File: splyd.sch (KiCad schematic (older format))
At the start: 74 parts, among them J0 AudioJack3, J1 USB from Pro micro, K00 KEYSW, K01 KEYSW, K02 KEYSW, K03 KEYSW, K04 KEYSW, K05 KEYSW, K10 KEYSW, K11 KEYSW, K12 KEYSW, K13 KEYSW, K14 KEYSW, K15 KEYSW, K16 KEYSW, K20 KEYSW, K21 KEYSW, K22 KEYSW, K23 KEYSW, K24 KEYSW, K25 KEYSW, K26 KEYSW, K30 KEYSW, K31 KEYSW, K32 KEYSW, K33 KEYSW, K34 KEYSW, K35 KEYSW, K36 KEYSW, K43 KEYSW, K44 KEYSW, K45 KEYSW, K46 KEYSW, K54 KEYSW, K55 KEYSW, K56 KEYSW, U0 Pro Micro

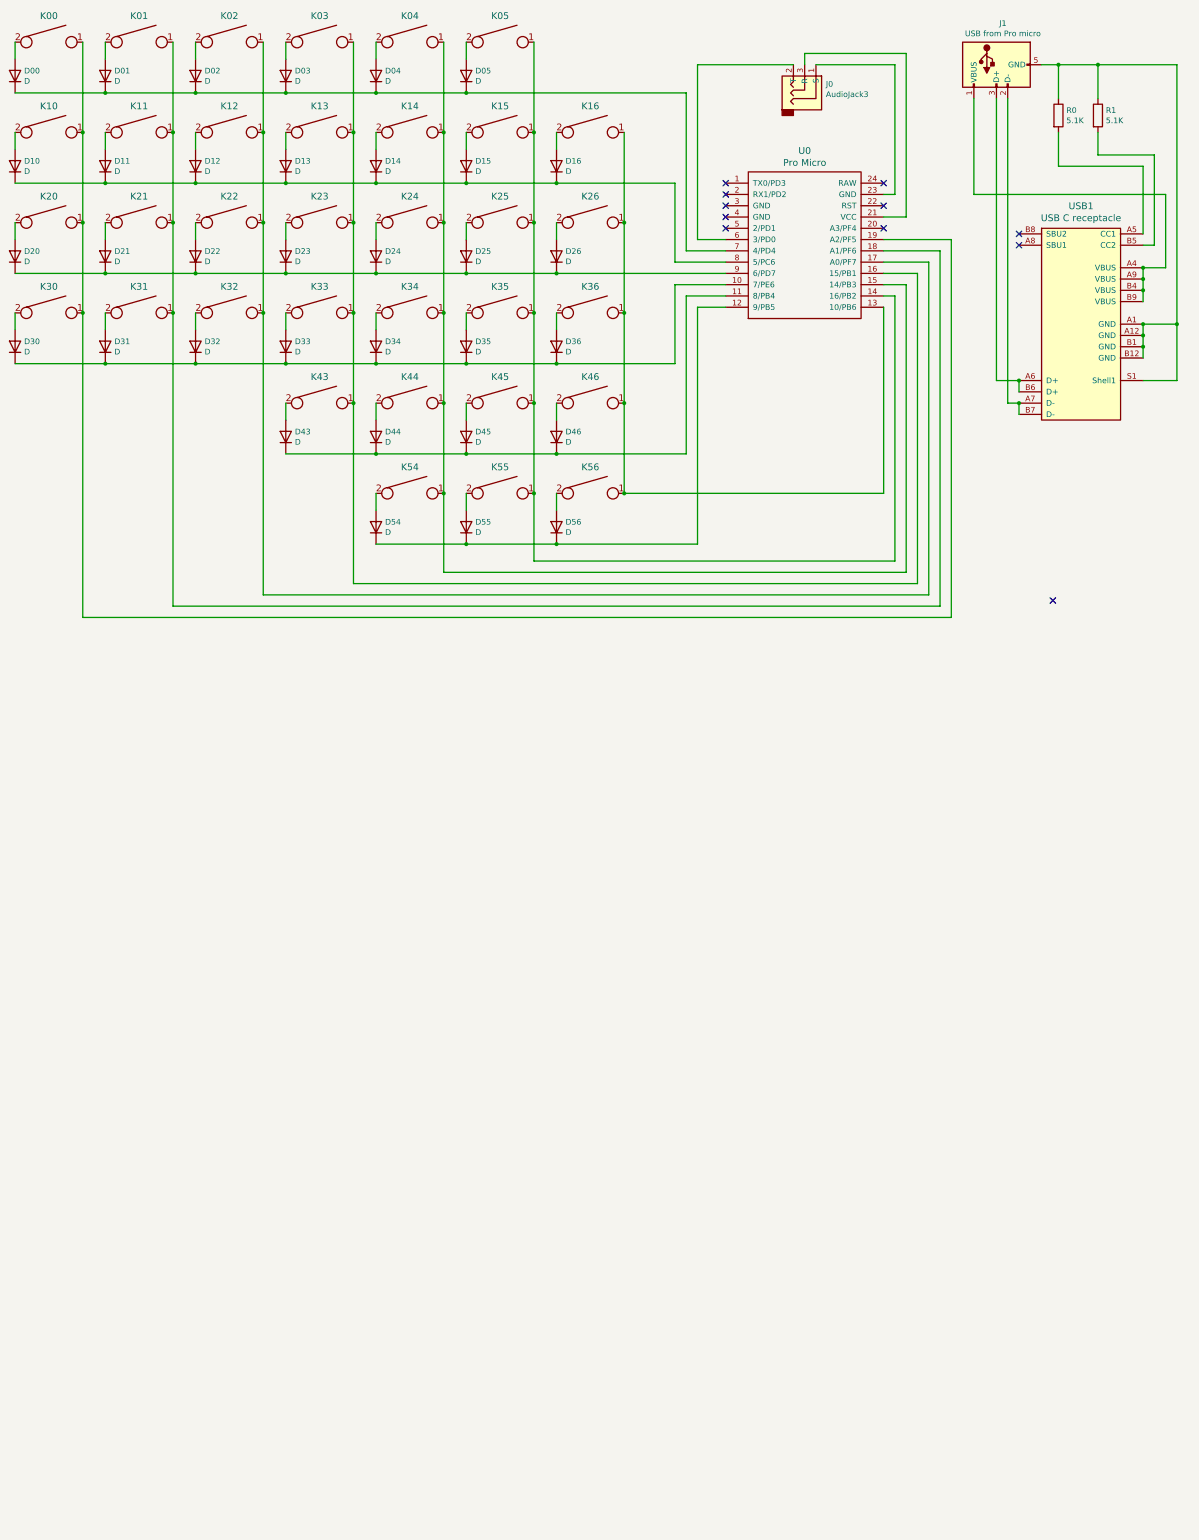
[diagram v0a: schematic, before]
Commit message: Add right hand and prepare footprint placements
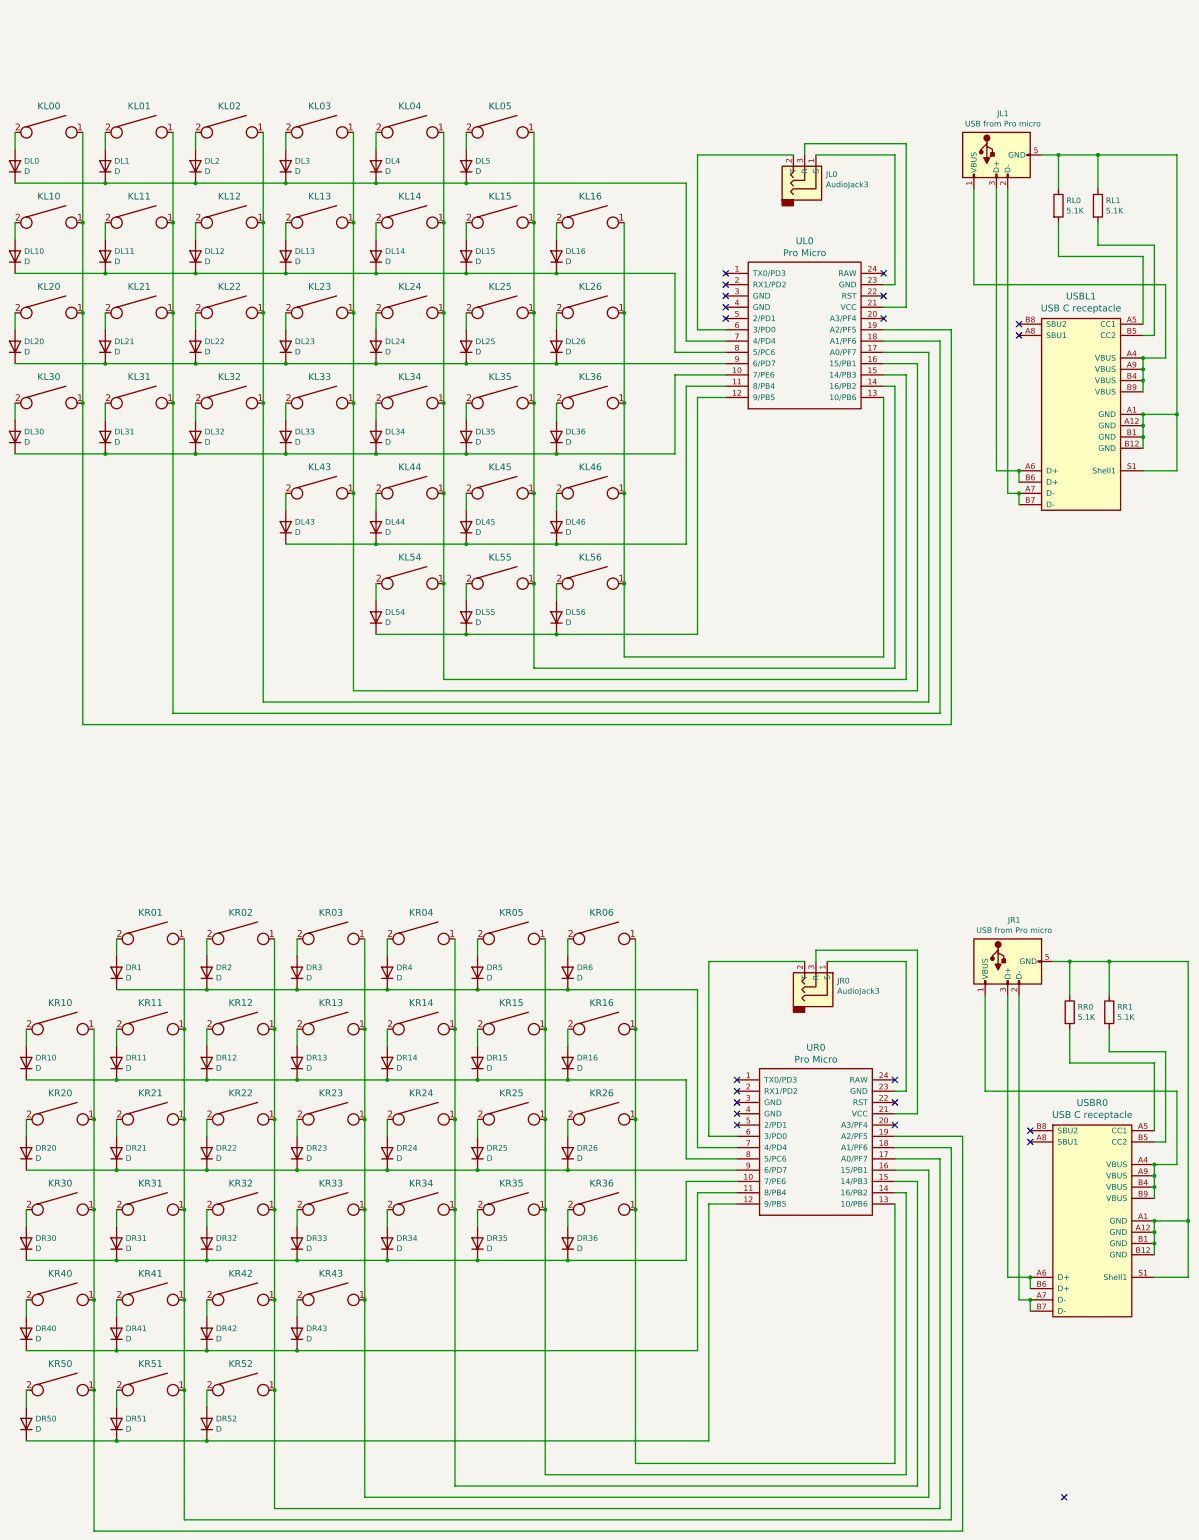
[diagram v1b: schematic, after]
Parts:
- added DR1, DR10, DR11, DR12, DR13, DR14, DR15, DR16, DR2, DR20, DR21, DR22, DR23, DR24, DR25, DR26, DR3, DR30, DR31, DR32, DR33, DR34, DR35, DR36, DR4, DR40, DR41, DR42, DR43, DR5, DR50, DR51, DR52, DR6: D, keyboard_parts:D_SOD123_axial, symbol Device:D
- added JR0: AudioJack3, mod_conn_av:jack_3.5_pj313d-smt, symbol Connector:AudioJack3
- added JR1: USB from Pro micro, Connector_Wire:Pad_1x04_SMD_1x2mm, symbol Connector:Micro_USB_wires
- added KR01, KR02, KR03, KR04, KR05, KR06, KR10, KR11, KR12, KR13, KR14, KR15, KR16, KR20, KR21, KR22, KR23, KR24, KR25, KR26, KR30, KR31, KR32, KR33, KR34, KR35, KR36, KR40, KR41, KR42, KR43, KR50, KR51, KR52: KEYSW, keyswitches:Kailh_socket_MX, symbol keyboard_parts:KEYSW
- added RR0, RR1: 5.1K, Resistor_SMD:R_0603_1608Metric, symbol Device:R
- added UR0: Pro Micro, Keebio-Parts:ArduinoProMicro-ZigZag, symbol keebio:ProMicro
- added USBR0: USB C receptacle, Type-C:USB_C_GCT_USB4085, symbol Type-C:USB_C_GCT_USB4085
- renumbered D00 to DL0, D01 to DL1, D10 to DL10, D11 to DL11, D12 to DL12, D13 to DL13, D14 to DL14, D15 to DL15, D16 to DL16, D02 to DL2, D20 to DL20, D21 to DL21, D22 to DL22, D23 to DL23, D24 to DL24, D25 to DL25, D26 to DL26, D03 to DL3, D30 to DL30, D31 to DL31, D32 to DL32, D33 to DL33, D34 to DL34, D35 to DL35, D36 to DL36, D04 to DL4, D43 to DL43, D44 to DL44, D45 to DL45, D46 to DL46, D05 to DL5, D54 to DL54, D55 to DL55, D56 to DL56, J0 to JL0, J1 to JL1, K00 to KL00, K01 to KL01, K02 to KL02, K03 to KL03, K04 to KL04, K05 to KL05, K10 to KL10, K11 to KL11, K12 to KL12, K13 to KL13, K14 to KL14, K15 to KL15, K16 to KL16, K20 to KL20, K21 to KL21, K22 to KL22, K23 to KL23, K24 to KL24, K25 to KL25, K26 to KL26, K30 to KL30, K31 to KL31, K32 to KL32, K33 to KL33, K34 to KL34, K35 to KL35, K36 to KL36, K43 to KL43, K44 to KL44, K45 to KL45, K46 to KL46, K54 to KL54, K55 to KL55, K56 to KL56, R0 to RL0, R1 to RL1, U0 to UL0, USB1 to USBL1
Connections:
- new net: JR1.5 (GND), RR0.1, RR1.1, USBR0.A1 (GND), USBR0.A12 (GND), USBR0.B1 (GND), USBR0.B12 (GND), USBR0.S1 (Shell1)
- new net: JR1.1 (VBUS), USBR0.A4 (VBUS), USBR0.A9 (VBUS), USBR0.B4 (VBUS), USBR0.B9 (VBUS)
- new net: RR0.2, USBR0.A5 (CC1)
- new net: JR1.3 (D+), USBR0.A6 (D+), USBR0.B6 (D+)
- new net: JR1.2 (D-), USBR0.A7 (D-), USBR0.B7 (D-)
- new net: RR1.2, USBR0.B5 (CC2)
- new net: DR30.1 (K), DR31.1 (K), DR32.1 (K), DR33.1 (K), DR34.1 (K), DR35.1 (K), DR36.1 (K), UR0.10 (7/PE6)
- new net: DR40.1 (K), DR41.1 (K), DR42.1 (K), DR43.1 (K), UR0.11 (8/PB4)
- new net: DR50.1 (K), DR51.1 (K), DR52.1 (K), UR0.12 (9/PB5)
- new net: KR06.1, KR16.1, KR26.1, KR36.1, UR0.13 (10/PB6)
- new net: KR05.1, KR15.1, KR25.1, KR35.1, UR0.14 (16/PB2)
- new net: KR04.1, KR14.1, KR24.1, KR34.1, UR0.15 (14/PB3)
- new net: KR03.1, KR13.1, KR23.1, KR33.1, KR43.1, UR0.16 (15/PB1)
- new net: KR02.1, KR12.1, KR22.1, KR32.1, KR42.1, KR52.1, UR0.17 (A0/PF7)
- new net: KR01.1, KR11.1, KR21.1, KR31.1, KR41.1, KR51.1, UR0.18 (A1/PF6)
- new net: KR10.1, KR20.1, KR30.1, KR40.1, KR50.1, UR0.19 (A2/PF5)
- new net: JR0.3 (R), UR0.21 (VCC)
- new net: JR0.1 (S), UR0.23 (GND)
- new net: JR0.2 (T), UR0.6 (3/PD0)
- new net: DR1.1 (K), DR2.1 (K), DR3.1 (K), DR4.1 (K), DR5.1 (K), DR6.1 (K), UR0.7 (4/PD4)
- new net: DR10.1 (K), DR11.1 (K), DR12.1 (K), DR13.1 (K), DR14.1 (K), DR15.1 (K), DR16.1 (K), UR0.8 (5/PC6)
- new net: DR20.1 (K), DR21.1 (K), DR22.1 (K), DR23.1 (K), DR24.1 (K), DR25.1 (K), DR26.1 (K), UR0.9 (6/PD7)
- new net: DR52.2 (A), KR52.2
- new net: DR43.2 (A), KR43.2
- new net: DR51.2 (A), KR51.2
- new net: DR50.2 (A), KR50.2
- new net: DR42.2 (A), KR42.2
- new net: DR41.2 (A), KR41.2
- new net: DR40.2 (A), KR40.2
- new net: DR36.2 (A), KR36.2
- new net: DR26.2 (A), KR26.2
- new net: DR35.2 (A), KR35.2
- new net: DR34.2 (A), KR34.2
- new net: DR25.2 (A), KR25.2
- new net: DR24.2 (A), KR24.2
- new net: DR33.2 (A), KR33.2
- new net: DR32.2 (A), KR32.2
- new net: DR23.2 (A), KR23.2
- new net: DR22.2 (A), KR22.2
- new net: DR31.2 (A), KR31.2
- new net: DR30.2 (A), KR30.2
- new net: DR21.2 (A), KR21.2
- new net: DR20.2 (A), KR20.2
- new net: DR16.2 (A), KR16.2
- new net: DR15.2 (A), KR15.2
- new net: DR14.2 (A), KR14.2
- new net: DR6.2 (A), KR06.2
- new net: DR5.2 (A), KR05.2
- new net: DR13.2 (A), KR13.2
- new net: DR12.2 (A), KR12.2
- new net: DR4.2 (A), KR04.2
- new net: DR3.2 (A), KR03.2
- new net: DR11.2 (A), KR11.2
- new net: DR10.2 (A), KR10.2
- new net: DR2.2 (A), KR02.2
- new net: DR1.2 (A), KR01.2
- no-connect marks 11 -> 21
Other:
- moved on the sheet: DL0, DL1, DL10, DL11, DL12, DL13, DL14, DL15, DL16, DL2, DL20, DL21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

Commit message: Keyswitch footprint with window and 3rd time routing
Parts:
- KL00, KL01, KL02, KL03, KL04, KL05, KL10, KL11, KL12, KL13, KL14, KL15, KL16, KL20, KL21, KL22, KL23, KL24, KL25, KL26, KL30, KL31, KL32, KL33, KL34, KL35, KL36, KL43, KL44, KL45, KL46, KL54, KL55, KL56, KR01, KR02, KR03, KR04, KR05, KR06, KR10, KR11, KR12, KR13, KR14, KR15, KR16, KR20, KR21, KR22, KR23, KR24, KR25, KR26, KR30, KR31, KR32, KR33, KR34, KR35, KR36, KR40, KR41, KR42, KR43, KR50, KR51, KR52: footprint keyswitches:Kailh_socket_MX -> keyswitches:Kailh_socket_MX--window

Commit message: Wire key RGB diodes for right thumb cluster
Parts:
- removed DL0, DL1, DL2, DL3, DL4, DL5, DR1, DR2, DR3, DR4, DR5, DR6: D, keyboard_parts:D_SOD123_axial, symbol Device:D
- removed KL00, KL01, KL02, KL03, KL04, KL05, KR01, KR02, KR03, KR04, KR05, KR06: KEYSW, keyswitches:Kailh_socket_MX--window, symbol keyboard_parts:KEYSW
- added CL00, CL01, CL02, CL03, CL04, CL05, CL06, CL10, CL11, CL12, CL13, CL14, CL15, CL16, CL20, CL21, CL22, CL23, CL24, CL25, CL26, CL33, CL34, CL35, CL36, CL44, CL45, CL46, CLBC_32, CLBL_33, CLBR_29, CLTC_31, CLTL_34, CLTR_30, CR00, CR01, CR02, CR03, CR04, CR05, CR06, CR10, CR11, CR12, CR13, CR14, CR15, CR16, CR20, CR21, CR22, CR23, CR24, CR25, CR26, CR30, CR31, CR32, CR33, CR40, CR41, CR42, CRBC_30, CRBL_29, CRBR_33, CRTC_31, CRTL_30, CRTR_34: C_Small, Capacitor_SMD:C_0603_1608Metric_Pad1.05x0.95mm_HandSolder, symbol Device:C_Small
- added DL00_1, DL01_6, DL02_7, DL03_12, DL04_13, DL05_18, DL06_19, DL10_2, DL11_5, DL12_8, DL13_11, DL14_14, DL15_17, DL16_20, DL20_3, DL21_4, DL22_9, DL23_10, DL24_15, DL25_16, DL26_21, DL33_28, DL34_27, DL35_24, DL36_23, DL44_26, DL45_25, DL46_22, DR00_19, DR01_18, DR02_13, DR03_12, DR04_7, DR05_6, DR06_1, DR10_20, DR11_17, DR12_14, DR13_11, DR14_8, DR15_5, DR16_2, DR20_21, DR21_16, DR22_15, DR23_10, DR24_9, DR25_4, DR26_3, DR30_23, DR31_24, DR32_27, DR33_28, DR40_22, DR41_25, DR42_26: SK6812MINI, keyboard_parts:SK6812MINIE-simple, symbol LED:SK6812MINI
- added DLBC_32, DLBL_33, DLBR_29, DLTC_31, DLTL_34, DLTR_30, DRBC_32, DRBL_29, DRBR_33, DRTC_31, DRTL_30, DRTR_34: SK6812MINI, keyboard_parts:SK6812MINIE-simple_no-hole, symbol LED:SK6812MINI
- JL0, JR0: footprint mod_conn_av:jack_3.5_pj313d-smt -> Keebio-Parts:TRS-PJ-320B
- KL00: renamed from KL10; footprint keyswitches:Kailh_socket_MX--window -> keyswitches:Kailh_socket_MX--space
- KL01: renamed from KL11; footprint keyswitches:Kailh_socket_MX--window -> keyswitches:Kailh_socket_MX--space
- KL02: renamed from KL12; footprint keyswitches:Kailh_socket_MX--window -> keyswitches:Kailh_socket_MX--space
- KL03: renamed from KL13; footprint keyswitches:Kailh_socket_MX--window -> keyswitches:Kailh_socket_MX--space
- KL04: renamed from KL14; footprint keyswitches:Kailh_socket_MX--window -> keyswitches:Kailh_socket_MX--space
- KL05: renamed from KL15; footprint keyswitches:Kailh_socket_MX--window -> keyswitches:Kailh_socket_MX--space
- KL06: renamed from KL16; footprint keyswitches:Kailh_socket_MX--window -> keyswitches:Kailh_socket_MX--space
- KL10: renamed from KL20; footprint keyswitches:Kailh_socket_MX--window -> keyswitches:Kailh_socket_MX--space
- KL11: renamed from KL21; footprint keyswitches:Kailh_socket_MX--window -> keyswitches:Kailh_socket_MX--space
- KL12: renamed from KL22; footprint keyswitches:Kailh_socket_MX--window -> keyswitches:Kailh_socket_MX--space
- KL13: renamed from KL23; footprint keyswitches:Kailh_socket_MX--window -> keyswitches:Kailh_socket_MX--space
- KL14: renamed from KL24; footprint keyswitches:Kailh_socket_MX--window -> keyswitches:Kailh_socket_MX--space
- KL15: renamed from KL25; footprint keyswitches:Kailh_socket_MX--window -> keyswitches:Kailh_socket_MX--space
- KL16: renamed from KL26; footprint keyswitches:Kailh_socket_MX--window -> keyswitches:Kailh_socket_MX--space
- KL20: renamed from KL30; footprint keyswitches:Kailh_socket_MX--window -> keyswitches:Kailh_socket_MX--space
- KL21: renamed from KL31; footprint keyswitches:Kailh_socket_MX--window -> keyswitches:Kailh_socket_MX--space
- KL22: renamed from KL32; footprint keyswitches:Kailh_socket_MX--window -> keyswitches:Kailh_socket_MX--space
- KL23: renamed from KL33; footprint keyswitches:Kailh_socket_MX--window -> keyswitches:Kailh_socket_MX--space
- KL24: renamed from KL34; footprint keyswitches:Kailh_socket_MX--window -> keyswitches:Kailh_socket_MX--space
- KL25: renamed from KL35; footprint keyswitches:Kailh_socket_MX--window -> keyswitches:Kailh_socket_MX--space
- KL26: renamed from KL36; footprint keyswitches:Kailh_socket_MX--window -> keyswitches:Kailh_socket_MX--space
- KL33: renamed from KL43; footprint keyswitches:Kailh_socket_MX--window -> keyswitches:Kailh_socket_MX--space
- KL34: renamed from KL44; footprint keyswitches:Kailh_socket_MX--window -> keyswitches:Kailh_socket_MX--space
- KL35: renamed from KL45; footprint keyswitches:Kailh_socket_MX--window -> keyswitches:Kailh_socket_MX--space
- KL36: renamed from KL46; footprint keyswitches:Kailh_socket_MX--window -> keyswitches:Kailh_socket_MX--space
- KL44: renamed from KL54; footprint keyswitches:Kailh_socket_MX--window -> keyswitches:Kailh_socket_MX--space
- KL45: renamed from KL55; footprint keyswitches:Kailh_socket_MX--window -> keyswitches:Kailh_socket_MX--space
- KL46: renamed from KL56; footprint keyswitches:Kailh_socket_MX--window -> keyswitches:Kailh_socket_MX--space
- KR00: renamed from KR10; footprint keyswitches:Kailh_socket_MX--window -> keyswitches:Kailh_socket_MX--space
- KR01: renamed from KR11; footprint keyswitches:Kailh_socket_MX--window -> keyswitches:Kailh_socket_MX--space
- KR02: renamed from KR12; footprint keyswitches:Kailh_socket_MX--window -> keyswitches:Kailh_socket_MX--space
- KR03: renamed from KR13; footprint keyswitches:Kailh_socket_MX--window -> keyswitches:Kailh_socket_MX--space
- KR04: renamed from KR14; footprint keyswitches:Kailh_socket_MX--window -> keyswitches:Kailh_socket_MX--space
- KR05: renamed from KR15; footprint keyswitches:Kailh_socket_MX--window -> keyswitches:Kailh_socket_MX--space
- KR06: renamed from KR16; footprint keyswitches:Kailh_socket_MX--window -> keyswitches:Kailh_socket_MX--space
- KR10: renamed from KR20; footprint keyswitches:Kailh_socket_MX--window -> keyswitches:Kailh_socket_MX--space
- KR11: renamed from KR21; footprint keyswitches:Kailh_socket_MX--window -> keyswitches:Kailh_socket_MX--space
- KR12: renamed from KR22; footprint keyswitches:Kailh_socket_MX--window -> keyswitches:Kailh_socket_MX--space
- KR13: renamed from KR23; footprint keyswitches:Kailh_socket_MX--window -> keyswitches:Kailh_socket_MX--space
- KR14: renamed from KR24; footprint keyswitches:Kailh_socket_MX--window -> keyswitches:Kailh_socket_MX--space
- KR15: renamed from KR25; footprint keyswitches:Kailh_socket_MX--window -> keyswitches:Kailh_socket_MX--space
- KR16: renamed from KR26; footprint keyswitches:Kailh_socket_MX--window -> keyswitches:Kailh_socket_MX--space
- KR20: renamed from KR30; footprint keyswitches:Kailh_socket_MX--window -> keyswitches:Kailh_socket_MX--space
- KR21: renamed from KR31; footprint keyswitches:Kailh_socket_MX--window -> keyswitches:Kailh_socket_MX--space
- KR22: renamed from KR32; footprint keyswitches:Kailh_socket_MX--window -> keyswitches:Kailh_socket_MX--space
- KR23: renamed from KR33; footprint keyswitches:Kailh_socket_MX--window -> keyswitches:Kailh_socket_MX--space
- KR24: renamed from KR34; footprint keyswitches:Kailh_socket_MX--window -> keyswitches:Kailh_socket_MX--space
- KR25: renamed from KR35; footprint keyswitches:Kailh_socket_MX--window -> keyswitches:Kailh_socket_MX--space
- KR26: renamed from KR36; footprint keyswitches:Kailh_socket_MX--window -> keyswitches:Kailh_socket_MX--space
- KR30: renamed from KR40; footprint keyswitches:Kailh_socket_MX--window -> keyswitches:Kailh_socket_MX--space
- KR31: renamed from KR41; footprint keyswitches:Kailh_socket_MX--window -> keyswitches:Kailh_socket_MX--space
- KR32: renamed from KR42; footprint keyswitches:Kailh_socket_MX--window -> keyswitches:Kailh_socket_MX--space
- KR33: renamed from KR43; footprint keyswitches:Kailh_socket_MX--window -> keyswitches:Kailh_socket_MX--space
- KR40: renamed from KR50; footprint keyswitches:Kailh_socket_MX--window -> keyswitches:Kailh_socket_MX--space
- KR41: renamed from KR51; footprint keyswitches:Kailh_socket_MX--window -> keyswitches:Kailh_socket_MX--space
- KR42: renamed from KR52; footprint keyswitches:Kailh_socket_MX--window -> keyswitches:Kailh_socket_MX--space
- renumbered DL10 to DL00, DL11 to DL01, DL12 to DL02, DL13 to DL03, DL14 to DL04, DL15 to DL05, DL16 to DL06, DL20 to DL10, DL21 to DL11, DL22 to DL12, DL23 to DL13, DL24 to DL14, DL25 to DL15, DL26 to DL16, DL30 to DL20, DL31 to DL21, DL32 to DL22, DL33 to DL23, DL34 to DL24, DL35 to DL25, DL36 to DL26, DL43 to DL33, DL44 to DL34, DL45 to DL35, DL46 to DL36, DL54 to DL44, DL55 to DL45, DL56 to DL46, DR10 to DR00, DR11 to DR01, DR12 to DR02, DR13 to DR03, DR14 to DR04, DR15 to DR05, DR16 to DR06, DR20 to DR10, DR21 to DR11, DR22 to DR12, DR23 to DR13, DR24 to DR14, DR25 to DR15, DR26 to DR16, DR30 to DR20, DR31 to DR21, DR32 to DR22, DR33 to DR23, DR34 to DR24, DR35 to DR25, DR36 to DR26, DR40 to DR30, DR41 to DR31, DR42 to DR32, DR43 to DR33, DR50 to DR40, DR51 to DR41, DR52 to DR42
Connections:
- net LLED: now reaches UL0.1 (TX0/PD3)
- net LLED: now also DLBR_29.3 (DIN)
- net L5V: now reaches JL0.3 (R), UL0.21 (VCC)
- net L5V: now also CL00.1, CL01.1, CL02.1, CL03.1, CL04.1, CL05.1, CL06.1, CL10.1, CL11.1, CL12.1, CL13.1, CL14.1, CL15.1, CL16.1, CL20.1, CL21.1, CL22.1, CL23.1, CL24.1, CL25.1, CL26.1, CL33.1, CL34.1, CL35.1, CL36.1, CL44.1, CL45.1, CL46.1, CLBC_32.1, CLBL_33.1, CLBR_29.1, CLTC_31.1, CLTL_34.1, CLTR_30.1, DL00_1.4 (VDD), DL01_6.4 (VDD), DL02_7.4 (VDD), DL03_12.4 (VDD), DL04_13.4 (VDD), DL05_18.4 (VDD), DL06_19.4 (VDD), DL10_2.4 (VDD), DL11_5.4 (VDD), DL12_8.4 (VDD), DL13_11.4 (VDD), DL14_14.4 (VDD), DL15_17.4 (VDD), DL16_20.4 (VDD), DL20_3.4 (VDD), DL21_4.4 (VDD), DL22_9.4 (VDD), DL23_10.4 (VDD), DL24_15.4 (VDD), DL25_16.4 (VDD), DL26_21.4 (VDD), DL33_28.4 (VDD), DL34_27.4 (VDD), DL35_24.4 (VDD), DL36_23.4 (VDD), DL44_26.4 (VDD), DL45_25.4 (VDD), DL46_22.4 (VDD), DLBC_32.4 (VDD), DLBL_33.4 (VDD), DLBR_29.4 (VDD), DLTC_31.4 (VDD), DLTL_34.4 (VDD), DLTR_30.4 (VDD)
- net GND1: now reaches JL0.1 (S), UL0.23 (GND)
- net GND1: now also CL00.2, CL01.2, CL02.2, CL03.2, CL04.2, CL05.2, CL06.2, CL10.2, CL11.2, CL12.2, CL13.2, CL14.2, CL15.2, CL16.2, CL20.2, CL21.2, CL22.2, CL23.2, CL24.2, CL25.2, CL26.2, CL33.2, CL34.2, CL35.2, CL36.2, CL44.2, CL45.2, CL46.2, CLBC_32.2, CLBL_33.2, CLBR_29.2, CLTC_31.2, CLTL_34.2, CLTR_30.2, DL00_1.2 (VSS), DL01_6.2 (VSS), DL02_7.2 (VSS), DL03_12.2 (VSS), DL04_13.2 (VSS), DL05_18.2 (VSS), DL06_19.2 (VSS), DL10_2.2 (VSS), DL11_5.2 (VSS), DL12_8.2 (VSS), DL13_11.2 (VSS), DL14_14.2 (VSS), DL15_17.2 (VSS), DL16_20.2 (VSS), DL20_3.2 (VSS), DL21_4.2 (VSS), DL22_9.2 (VSS), DL23_10.2 (VSS), DL24_15.2 (VSS), DL25_16.2 (VSS), DL26_21.2 (VSS), DL33_28.2 (VSS), DL34_27.2 (VSS), DL35_24.2 (VSS), DL36_23.2 (VSS), DL44_26.2 (VSS), DL45_25.2 (VSS), DL46_22.2 (VSS), DLBC_32.2 (VSS), DLBL_33.2 (VSS), DLBR_29.2 (VSS), DLTC_31.2 (VSS), DLTL_34.2 (VSS), DLTR_30.2 (VSS)
- net RLED: now reaches UR0.1 (TX0/PD3)
- net RLED: now also DRBL_29.3 (DIN)
- net R5V: now reaches JR0.3 (R), UR0.21 (VCC)
- net R5V: now also CR00.1, CR01.1, CR02.1, CR03.1, CR04.1, CR05.1, CR06.1, CR10.1, CR11.1, CR12.1, CR13.1, CR14.1, CR15.1, CR16.1, CR20.1, CR21.1, CR22.1, CR23.1, CR24.1, CR25.1, CR26.1, CR30.1, CR31.1, CR32.1, CR33.1, CR40.1, CR41.1, CR42.1, CRBC_30.1, CRBL_29.1, CRBR_33.1, CRTC_31.1, CRTL_30.1, CRTR_34.1, DR00_19.4 (VDD), DR01_18.4 (VDD), DR02_13.4 (VDD), DR03_12.4 (VDD), DR04_7.4 (VDD), DR05_6.4 (VDD), DR06_1.4 (VDD), DR10_20.4 (VDD), DR11_17.4 (VDD), DR12_14.4 (VDD), DR13_11.4 (VDD), DR14_8.4 (VDD), DR15_5.4 (VDD), DR16_2.4 (VDD), DR20_21.4 (VDD), DR21_16.4 (VDD), DR22_15.4 (VDD), DR23_10.4 (VDD), DR24_9.4 (VDD), DR25_4.4 (VDD), DR26_3.4 (VDD), DR30_23.4 (VDD), DR31_24.4 (VDD), DR32_27.4 (VDD), DR33_28.4 (VDD), DR40_22.4 (VDD), DR41_25.4 (VDD), DR42_26.4 (VDD), DRBC_32.4 (VDD), DRBL_29.4 (VDD), DRBR_33.4 (VDD), DRTC_31.4 (VDD), DRTL_30.4 (VDD), DRTR_34.4 (VDD)
- net GND2: now reaches JR0.1 (S), UR0.23 (GND)
- net GND2: now also CR00.2, CR01.2, CR02.2, CR03.2, CR04.2, CR05.2, CR06.2, CR10.2, CR11.2, CR12.2, CR13.2, CR14.2, CR15.2, CR16.2, CR20.2, CR21.2, CR22.2, CR23.2, CR24.2, CR25.2, CR26.2, CR30.2, CR31.2, CR32.2, CR33.2, CR40.2, CR41.2, CR42.2, CRBC_30.2, CRBL_29.2, CRBR_33.2, CRTC_31.2, CRTL_30.2, CRTR_34.2, DR00_19.2 (VSS), DR01_18.2 (VSS), DR02_13.2 (VSS), DR03_12.2 (VSS), DR04_7.2 (VSS), DR05_6.2 (VSS), DR06_1.2 (VSS), DR10_20.2 (VSS), DR11_17.2 (VSS), DR12_14.2 (VSS), DR13_11.2 (VSS), DR14_8.2 (VSS), DR15_5.2 (VSS), DR16_2.2 (VSS), DR20_21.2 (VSS), DR21_16.2 (VSS), DR22_15.2 (VSS), DR23_10.2 (VSS), DR24_9.2 (VSS), DR25_4.2 (VSS), DR26_3.2 (VSS), DR30_23.2 (VSS), DR31_24.2 (VSS), DR32_27.2 (VSS), DR33_28.2 (VSS), DR40_22.2 (VSS), DR41_25.2 (VSS), DR42_26.2 (VSS), DRBC_32.2 (VSS), DRBL_29.2 (VSS), DRBR_33.2 (VSS), DRTC_31.2 (VSS), DRTL_30.2 (VSS), DRTR_34.2 (VSS)
- new net: DL00_1.1 (DOUT), DL10_2.3 (DIN)
- new net: DL00_1.3 (DIN), DLTL_34.1 (DOUT)
- new net: DL10_2.1 (DOUT), DL20_3.3 (DIN)
- new net: DL20_3.1 (DOUT), DL21_4.3 (DIN)
- new net: DL01_6.1 (DOUT), DL02_7.3 (DIN)
- new net: DL01_6.3 (DIN), DL11_5.1 (DOUT)
- new net: DL11_5.3 (DIN), DL21_4.1 (DOUT)
- new net: DL02_7.1 (DOUT), DL12_8.3 (DIN)
- new net: DL12_8.1 (DOUT), DL22_9.3 (DIN)
- new net: DL22_9.1 (DOUT), DL23_10.3 (DIN)
- new net: DL03_12.1 (DOUT), DL04_13.3 (DIN)
- new net: DL03_12.3 (DIN), DL13_11.1 (DOUT)
- new net: DL13_11.3 (DIN), DL23_10.1 (DOUT)
- new net: DL33_28.3 (DIN), DL34_27.1 (DOUT)
- new net: DL04_13.1 (DOUT), DL14_14.3 (DIN)
- new net: DL14_14.1 (DOUT), DL24_15.3 (DIN)
- new net: DL24_15.1 (DOUT), DL25_16.3 (DIN)
- new net: DL34_27.3 (DIN), DL44_26.1 (DOUT)
- new net: DL44_26.3 (DIN), DL45_25.1 (DOUT)
- new net: DL05_18.1 (DOUT), DL06_19.3 (DIN)
- new net: DL05_18.3 (DIN), DL15_17.1 (DOUT)
- new net: DL15_17.3 (DIN), DL25_16.1 (DOUT)
- new net: DL35_24.1 (DOUT), DL45_25.3 (DIN)
- new net: DL35_24.3 (DIN), DL36_23.1 (DOUT)
- new net: DL06_19.1 (DOUT), DL16_20.3 (DIN)
- new net: DL16_20.1 (DOUT), DL26_21.3 (DIN)
- new net: DL26_21.1 (DOUT), DL46_22.3 (DIN)
- new net: DL36_23.3 (DIN), DL46_22.1 (DOUT)
- new net: DLBL_33.1 (DOUT), DLTL_34.3 (DIN)
- new net: DLBC_32.1 (DOUT), DLBL_33.3 (DIN)
- new net: DLBC_32.3 (DIN), DLTC_31.1 (DOUT)
- new net: DLTC_31.3 (DIN), DLTR_30.1 (DOUT)
- new net: DLBR_29.1 (DOUT), DLTR_30.3 (DIN)
- new net: DR00_19.1 (DOUT), DR10_20.3 (DIN)
- new net: DR00_19.3 (DIN), DR01_18.1 (DOUT)
- new net: DR10_20.1 (DOUT), DR20_21.3 (DIN)
- new net: DR20_21.1 (DOUT), DR40_22.3 (DIN)
- new net: DR30_23.1 (DOUT), DR31_24.3 (DIN)
- new net: DR30_23.3 (DIN), DR40_22.1 (DOUT)
- new net: DR01_18.3 (DIN), DR11_17.1 (DOUT)
- new net: DR11_17.3 (DIN), DR21_16.1 (DOUT)
- new net: DR21_16.3 (DIN), DR22_15.1 (DOUT)
- new net: DR31_24.1 (DOUT), DR41_25.3 (DIN)
- new net: DR41_25.1 (DOUT), DR42_26.3 (DIN)
- new net: DR02_13.1 (DOUT), DR12_14.3 (DIN)
- new net: DR02_13.3 (DIN), DR03_12.1 (DOUT)
- new net: DR12_14.1 (DOUT), DR22_15.3 (DIN)
- new net: DR32_27.1 (DOUT), DR33_28.3 (DIN)
- new net: DR32_27.3 (DIN), DR42_26.1 (DOUT)
- new net: DR03_12.3 (DIN), DR13_11.1 (DOUT)
- new net: DR13_11.3 (DIN), DR23_10.1 (DOUT)
- new net: DR23_10.3 (DIN), DR24_9.1 (DOUT)
- new net: DR04_7.1 (DOUT), DR14_8.3 (DIN)
- new net: DR04_7.3 (DIN), DR05_6.1 (DOUT)
- new net: DR14_8.1 (DOUT), DR24_9.3 (DIN)
- new net: DR05_6.3 (DIN), DR15_5.1 (DOUT)
- new net: DR15_5.3 (DIN), DR25_4.1 (DOUT)
- new net: DR25_4.3 (DIN), DR26_3.1 (DOUT)
- new net: DR06_1.1 (DOUT), DR16_2.3 (DIN)
- new net: DR06_1.3 (DIN), DRTR_34.1 (DOUT)
- new net: DR16_2.1 (DOUT), DR26_3.3 (DIN)
- new net: DRTC_31.3 (DIN), DRTL_30.1 (DOUT)
- new net: DRBL_29.1 (DOUT), DRTL_30.3 (DIN)
- new net: DRBC_32.3 (DIN), DRTC_31.1 (DOUT)
- new net: DRBC_32.1 (DOUT), DRBR_33.3 (DIN)
- new net: DRBR_33.1 (DOUT), DRTR_34.3 (DIN)
- no-connect marks 21 -> 22
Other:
- moved on the sheet: DL00, DL01, DL02, DL03, DL04, DL05, DL06, DL10, DL11, DL12, DL13, DL14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

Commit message: Fix SK6812MINI-E schema
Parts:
- DL00_1, DL01_6, DL02_7, DL03_12, DL04_13, DL05_18, DL06_19, DL10_2, DL11_5, DL12_8, DL13_11, DL14_14, DL15_17, DL16_20, DL20_3, DL21_4, DL22_9, DL23_10, DL24_15, DL25_16, DL26_21, DL33_28, DL34_27, DL35_24, DL36_23, DL44_26, DL45_25, DL46_22, DLBC_32, DLBL_33, DLBR_29, DLTC_31, DLTL_34, DLTR_30, DR00_19, DR01_18, DR02_13, DR03_12, DR04_7, DR05_6, DR06_1, DR10_20, DR11_17, DR12_14, DR13_11, DR14_8, DR15_5, DR16_2, DR20_21, DR21_16, DR22_15, DR23_10, DR24_9, DR25_4, DR26_3, DR30_23, DR31_24, DR32_27, DR33_28, DR40_22, DR41_25, DR42_26, DRBC_32, DRBL_29, DRBR_33, DRTC_31, DRTL_30, DRTR_34: value SK6812MINI -> SK6812MINI-E; symbol LED:SK6812MINI -> LED:SK6812MINI-E
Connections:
- net GND1: now also DL00_1.3 (GND), DL01_6.3 (GND), DL02_7.3 (GND), DL03_12.3 (GND), DL04_13.3 (GND), DL05_18.3 (GND), DL06_19.3 (GND), DL10_2.3 (GND), DL11_5.3 (GND), DL12_8.3 (GND), DL13_11.3 (GND), DL14_14.3 (GND), DL15_17.3 (GND), DL16_20.3 (GND), DL20_3.3 (GND), DL21_4.3 (GND), DL22_9.3 (GND), DL23_10.3 (GND), DL24_15.3 (GND), DL25_16.3 (GND), DL26_21.3 (GND), DL33_28.3 (GND), DL34_27.3 (GND), DL35_24.3 (GND), DL36_23.3 (GND), DL44_26.3 (GND), DL45_25.3 (GND), DL46_22.3 (GND), DLBC_32.3 (GND), DLBL_33.3 (GND), DLBR_29.3 (GND), DLTC_31.3 (GND), DLTL_34.3 (GND), DLTR_30.3 (GND); no longer DL00_1.2 (VSS), DL01_6.2 (VSS), DL02_7.2 (VSS), DL03_12.2 (VSS), DL04_13.2 (VSS), DL05_18.2 (VSS), DL06_19.2 (VSS), DL10_2.2 (VSS), DL11_5.2 (VSS), DL12_8.2 (VSS), DL13_11.2 (VSS), DL14_14.2 (VSS), DL15_17.2 (VSS), DL16_20.2 (VSS), DL20_3.2 (VSS), DL21_4.2 (VSS), DL22_9.2 (VSS), DL23_10.2 (VSS), DL24_15.2 (VSS), DL25_16.2 (VSS), DL26_21.2 (VSS), DL33_28.2 (VSS), DL34_27.2 (VSS), DL35_24.2 (VSS), DL36_23.2 (VSS), DL44_26.2 (VSS), DL45_25.2 (VSS), DL46_22.2 (VSS), DLBC_32.2 (VSS), DLBL_33.2 (VSS), DLBR_29.2 (VSS), DLTC_31.2 (VSS), DLTL_34.2 (VSS), DLTR_30.2 (VSS)
- net GND2: now also DR00_19.3 (GND), DR01_18.3 (GND), DR02_13.3 (GND), DR03_12.3 (GND), DR04_7.3 (GND), DR05_6.3 (GND), DR06_1.3 (GND), DR10_20.3 (GND), DR11_17.3 (GND), DR12_14.3 (GND), DR13_11.3 (GND), DR14_8.3 (GND), DR15_5.3 (GND), DR16_2.3 (GND), DR20_21.3 (GND), DR21_16.3 (GND), DR22_15.3 (GND), DR23_10.3 (GND), DR24_9.3 (GND), DR25_4.3 (GND), DR26_3.3 (GND), DR30_23.3 (GND), DR31_24.3 (GND), DR32_27.3 (GND), DR33_28.3 (GND), DR40_22.3 (GND), DR41_25.3 (GND), DR42_26.3 (GND), DRBC_32.3 (GND), DRBL_29.3 (GND), DRBR_33.3 (GND), DRTC_31.3 (GND), DRTL_30.3 (GND), DRTR_34.3 (GND); no longer DR00_19.2 (VSS), DR01_18.2 (VSS), DR02_13.2 (VSS), DR03_12.2 (VSS), DR04_7.2 (VSS), DR05_6.2 (VSS), DR06_1.2 (VSS), DR10_20.2 (VSS), DR11_17.2 (VSS), DR12_14.2 (VSS), DR13_11.2 (VSS), DR14_8.2 (VSS), DR15_5.2 (VSS), DR16_2.2 (VSS), DR20_21.2 (VSS), DR21_16.2 (VSS), DR22_15.2 (VSS), DR23_10.2 (VSS), DR24_9.2 (VSS), DR25_4.2 (VSS), DR26_3.2 (VSS), DR30_23.2 (VSS), DR31_24.2 (VSS), DR32_27.2 (VSS), DR33_28.2 (VSS), DR40_22.2 (VSS), DR41_25.2 (VSS), DR42_26.2 (VSS), DRBC_32.2 (VSS), DRBL_29.2 (VSS), DRBR_33.2 (VSS), DRTC_31.2 (VSS), DRTL_30.2 (VSS), DRTR_34.2 (VSS)
- net L5V: now also DL00_1.1 (VDD), DL01_6.1 (VDD), DL02_7.1 (VDD), DL03_12.1 (VDD), DL04_13.1 (VDD), DL05_18.1 (VDD), DL06_19.1 (VDD), DL10_2.1 (VDD), DL11_5.1 (VDD), DL12_8.1 (VDD), DL13_11.1 (VDD), DL14_14.1 (VDD), DL15_17.1 (VDD), DL16_20.1 (VDD), DL20_3.1 (VDD), DL21_4.1 (VDD), DL22_9.1 (VDD), DL23_10.1 (VDD), DL24_15.1 (VDD), DL25_16.1 (VDD), DL26_21.1 (VDD), DL33_28.1 (VDD), DL34_27.1 (VDD), DL35_24.1 (VDD), DL36_23.1 (VDD), DL44_26.1 (VDD), DL45_25.1 (VDD), DL46_22.1 (VDD), DLBC_32.1 (VDD), DLBL_33.1 (VDD), DLBR_29.1 (VDD), DLTC_31.1 (VDD), DLTL_34.1 (VDD), DLTR_30.1 (VDD); no longer DL00_1.4 (VDD), DL01_6.4 (VDD), DL02_7.4 (VDD), DL03_12.4 (VDD), DL04_13.4 (VDD), DL05_18.4 (VDD), DL06_19.4 (VDD), DL10_2.4 (VDD), DL11_5.4 (VDD), DL12_8.4 (VDD), DL13_11.4 (VDD), DL14_14.4 (VDD), DL15_17.4 (VDD), DL16_20.4 (VDD), DL20_3.4 (VDD), DL21_4.4 (VDD), DL22_9.4 (VDD), DL23_10.4 (VDD), DL24_15.4 (VDD), DL25_16.4 (VDD), DL26_21.4 (VDD), DL33_28.4 (VDD), DL34_27.4 (VDD), DL35_24.4 (VDD), DL36_23.4 (VDD), DL44_26.4 (VDD), DL45_25.4 (VDD), DL46_22.4 (VDD), DLBC_32.4 (VDD), DLBL_33.4 (VDD), DLBR_29.4 (VDD), DLTC_31.4 (VDD), DLTL_34.4 (VDD), DLTR_30.4 (VDD)
- net LLED: now also DLBR_29.4 (DIN); no longer DLBR_29.3 (DIN)
- net R5V: now also DR00_19.1 (VDD), DR01_18.1 (VDD), DR02_13.1 (VDD), DR03_12.1 (VDD), DR04_7.1 (VDD), DR05_6.1 (VDD), DR06_1.1 (VDD), DR10_20.1 (VDD), DR11_17.1 (VDD), DR12_14.1 (VDD), DR13_11.1 (VDD), DR14_8.1 (VDD), DR15_5.1 (VDD), DR16_2.1 (VDD), DR20_21.1 (VDD), DR21_16.1 (VDD), DR22_15.1 (VDD), DR23_10.1 (VDD), DR24_9.1 (VDD), DR25_4.1 (VDD), DR26_3.1 (VDD), DR30_23.1 (VDD), DR31_24.1 (VDD), DR32_27.1 (VDD), DR33_28.1 (VDD), DR40_22.1 (VDD), DR41_25.1 (VDD), DR42_26.1 (VDD), DRBC_32.1 (VDD), DRBL_29.1 (VDD), DRBR_33.1 (VDD), DRTC_31.1 (VDD), DRTL_30.1 (VDD), DRTR_34.1 (VDD); no longer DR00_19.4 (VDD), DR01_18.4 (VDD), DR02_13.4 (VDD), DR03_12.4 (VDD), DR04_7.4 (VDD), DR05_6.4 (VDD), DR06_1.4 (VDD), DR10_20.4 (VDD), DR11_17.4 (VDD), DR12_14.4 (VDD), DR13_11.4 (VDD), DR14_8.4 (VDD), DR15_5.4 (VDD), DR16_2.4 (VDD), DR20_21.4 (VDD), DR21_16.4 (VDD), DR22_15.4 (VDD), DR23_10.4 (VDD), DR24_9.4 (VDD), DR25_4.4 (VDD), DR26_3.4 (VDD), DR30_23.4 (VDD), DR31_24.4 (VDD), DR32_27.4 (VDD), DR33_28.4 (VDD), DR40_22.4 (VDD), DR41_25.4 (VDD), DR42_26.4 (VDD), DRBC_32.4 (VDD), DRBL_29.4 (VDD), DRBR_33.4 (VDD), DRTC_31.4 (VDD), DRTL_30.4 (VDD), DRTR_34.4 (VDD)
- net RLED: now also DRBL_29.4 (DIN); no longer DRBL_29.3 (DIN)
- new net: DL00_1.2 (DOUT), DL10_2.4 (DIN)
- new net: DL00_1.4 (DIN), DLTL_34.2 (DOUT)
- new net: DL10_2.2 (DOUT), DL20_3.4 (DIN)
- new net: DL20_3.2 (DOUT), DL21_4.4 (DIN)
- new net: DL01_6.2 (DOUT), DL02_7.4 (DIN)
- new net: DL01_6.4 (DIN), DL11_5.2 (DOUT)
- new net: DL11_5.4 (DIN), DL21_4.2 (DOUT)
- new net: DL02_7.2 (DOUT), DL12_8.4 (DIN)
- new net: DL12_8.2 (DOUT), DL22_9.4 (DIN)
- new net: DL22_9.2 (DOUT), DL23_10.4 (DIN)
- new net: DL03_12.2 (DOUT), DL04_13.4 (DIN)
- new net: DL03_12.4 (DIN), DL13_11.2 (DOUT)
- new net: DL13_11.4 (DIN), DL23_10.2 (DOUT)
- new net: DL33_28.4 (DIN), DL34_27.2 (DOUT)
- new net: DL04_13.2 (DOUT), DL14_14.4 (DIN)
- new net: DL14_14.2 (DOUT), DL24_15.4 (DIN)
- new net: DL24_15.2 (DOUT), DL25_16.4 (DIN)
- new net: DL34_27.4 (DIN), DL44_26.2 (DOUT)
- new net: DL44_26.4 (DIN), DL45_25.2 (DOUT)
- new net: DL05_18.2 (DOUT), DL06_19.4 (DIN)
- new net: DL05_18.4 (DIN), DL15_17.2 (DOUT)
- new net: DL15_17.4 (DIN), DL25_16.2 (DOUT)
- new net: DL35_24.2 (DOUT), DL45_25.4 (DIN)
- new net: DL35_24.4 (DIN), DL36_23.2 (DOUT)
- new net: DL06_19.2 (DOUT), DL16_20.4 (DIN)
- new net: DL16_20.2 (DOUT), DL26_21.4 (DIN)
- new net: DL26_21.2 (DOUT), DL46_22.4 (DIN)
- new net: DL36_23.4 (DIN), DL46_22.2 (DOUT)
- new net: DLBL_33.2 (DOUT), DLTL_34.4 (DIN)
- new net: DLBC_32.2 (DOUT), DLBL_33.4 (DIN)
- new net: DLBC_32.4 (DIN), DLTC_31.2 (DOUT)
- new net: DLTC_31.4 (DIN), DLTR_30.2 (DOUT)
- new net: DLBR_29.2 (DOUT), DLTR_30.4 (DIN)
- new net: DR00_19.2 (DOUT), DR10_20.4 (DIN)
- new net: DR00_19.4 (DIN), DR01_18.2 (DOUT)
- new net: DR10_20.2 (DOUT), DR20_21.4 (DIN)
- new net: DR20_21.2 (DOUT), DR40_22.4 (DIN)
- new net: DR30_23.2 (DOUT), DR31_24.4 (DIN)
- new net: DR30_23.4 (DIN), DR40_22.2 (DOUT)
- new net: DR01_18.4 (DIN), DR11_17.2 (DOUT)
- new net: DR11_17.4 (DIN), DR21_16.2 (DOUT)
- new net: DR21_16.4 (DIN), DR22_15.2 (DOUT)
- new net: DR31_24.2 (DOUT), DR41_25.4 (DIN)
- new net: DR41_25.2 (DOUT), DR42_26.4 (DIN)
- new net: DR02_13.2 (DOUT), DR12_14.4 (DIN)
- new net: DR02_13.4 (DIN), DR03_12.2 (DOUT)
- new net: DR12_14.2 (DOUT), DR22_15.4 (DIN)
- new net: DR32_27.2 (DOUT), DR33_28.4 (DIN)
- new net: DR32_27.4 (DIN), DR42_26.2 (DOUT)
- new net: DR03_12.4 (DIN), DR13_11.2 (DOUT)
- new net: DR13_11.4 (DIN), DR23_10.2 (DOUT)
- new net: DR23_10.4 (DIN), DR24_9.2 (DOUT)
- new net: DR04_7.2 (DOUT), DR14_8.4 (DIN)
- new net: DR04_7.4 (DIN), DR05_6.2 (DOUT)
- new net: DR14_8.2 (DOUT), DR24_9.4 (DIN)
- new net: DR05_6.4 (DIN), DR15_5.2 (DOUT)
- new net: DR15_5.4 (DIN), DR25_4.2 (DOUT)
- new net: DR25_4.4 (DIN), DR26_3.2 (DOUT)
- new net: DR06_1.2 (DOUT), DR16_2.4 (DIN)
- new net: DR06_1.4 (DIN), DRTR_34.2 (DOUT)
- new net: DR16_2.2 (DOUT), DR26_3.4 (DIN)
- new net: DRTC_31.4 (DIN), DRTL_30.2 (DOUT)
- new net: DRBL_29.2 (DOUT), DRTL_30.4 (DIN)
- new net: DRBC_32.4 (DIN), DRTC_31.2 (DOUT)
- new net: DRBC_32.2 (DOUT), DRBR_33.4 (DIN)
- new net: DRBR_33.2 (DOUT), DRTR_34.4 (DIN)
